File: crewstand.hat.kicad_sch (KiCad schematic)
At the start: 18 parts, among them J1 GPIO, J2 CAN Terminal, J3 Sensor Terminal, J4 V-In, J6 V-Out, J7 Relais2, J8 Relais1, U2 MCP2515-xSO, U3 MCP2551-I-P, U4 PicoW, Y2 12M

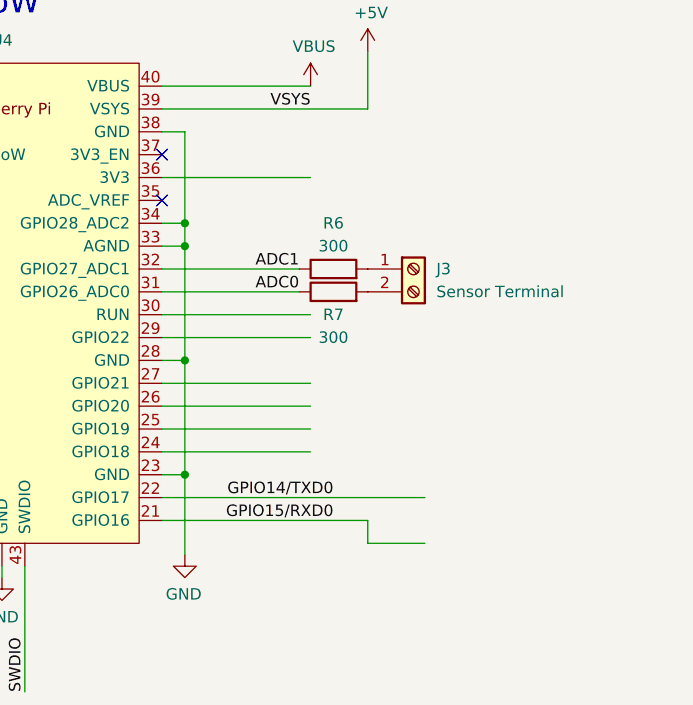
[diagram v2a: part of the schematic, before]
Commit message: fix(Sensors): correct resistor placement for analog sensor readings
- Move pull-down resistors from sensor-to-ADC path to ADC-to-GND
- Update schematic to implement proper current-to-voltage conversion

Breaking Change: Yes
- PCB layout updated
- Existing boards will need rework to implement this fix

Resolves: #6
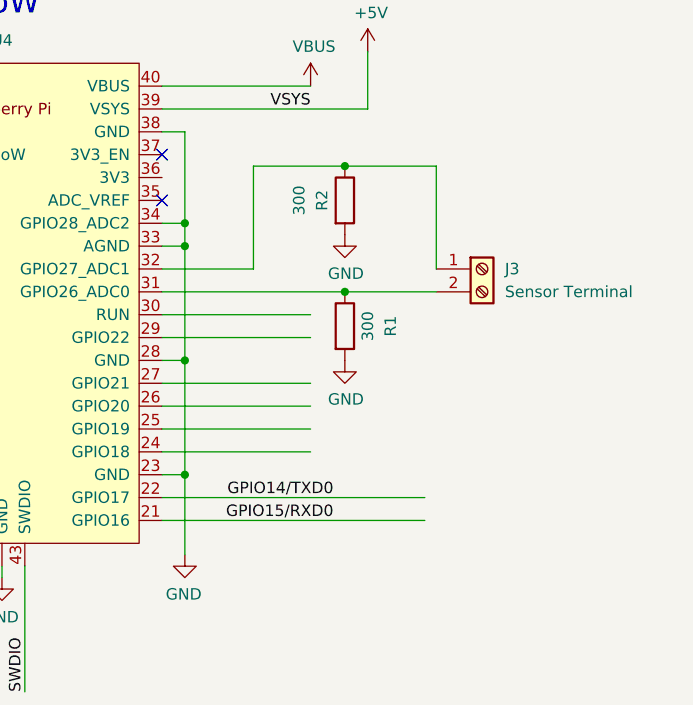
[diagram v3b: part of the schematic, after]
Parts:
- removed R6, R7: 300, Resistor_THT:R_Axial_DIN0204_L3.6mm_D1.6mm_P5.08mm_Horizontal, symbol Device:R
- added R1, R2: 300, Resistor_THT:R_Axial_DIN0204_L3.6mm_D1.6mm_P5.08mm_Horizontal, symbol Device:R
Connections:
- net ADC0 is gone; now on an unnamed net: U4.31 (GPIO26_ADC0)
- net ADC1 is gone; now on an unnamed net: U4.32 (GPIO27_ADC1)
- net GND: now also R1.2, R2.2
- net at J3.1 (Pin_1): now also R2.1
- net at J3.2 (Pin_2): now also R1.1
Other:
- moved on the sheet: J3
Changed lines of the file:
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@@
   (junction (at 179.07 128.27) (diameter 0) (color 0 0 0 0)
   )
+  (junction (at 259.08 38.1) (diameter 0) (color 0 0 0 0)
+  )
+  (junction (at 259.08 52.07) (diameter 0) (color 0 0 0 0)
+  )
   (no_connect (at 238.76 36.83))
   (no_connect (at 238.76 41.91))
@@
     (stroke (width 0) (type solid))
   )
+  (wire (pts (xy 248.92 38.1) (xy 259.08 38.1))
+    (stroke (width 0) (type default))
+  )
   (wire (pts (xy 96.52 125.73) (xy 104.14 125.73))
     (stroke (width 0) (type default))
@@
     (stroke (width 0) (type solid))
   )
+  (wire (pts (xy 248.92 38.1) (xy 248.92 49.53))
+    (stroke (width 0) (type default))
+  )
   (wire (pts (xy 60.96 30.48) (xy 31.75 30.48))
     (stroke (width 0) (type solid))
@@
     (stroke (width 0) (type solid))
   )
-  (wire (pts (xy 261.62 80.01) (xy 267.97 80.01))
-    (stroke (width 0) (type default))
-  )
-  (wire (pts (xy 261.62 77.47) (xy 261.62 80.01))
-    (stroke (width 0) (type default))
-  )
   (wire (pts (xy 73.66 40.64) (xy 100.33 40.64))
     (stroke (width 0) (type solid))
@@
     (stroke (width 0) (type solid))
   )
+  (wire (pts (xy 259.08 52.07) (xy 269.24 52.07))
+    (stroke (width 0) (type default))
+  )
   (wire (pts (xy 76.2 27.94) (xy 73.66 27.94))
     (stroke (width 0) (type solid))
@@
     (stroke (width 0) (type default))
   )
+  (wire (pts (xy 269.24 38.1) (xy 269.24 49.53))
+    (stroke (width 0) (type default))
+  )
   (wire (pts (xy 153.67 107.95) (xy 153.67 110.49))
     (stroke (width 0) (type default))
@@
     (stroke (width 0) (type default))
   )
-  (wire (pts (xy 238.76 49.53) (xy 254 49.53))
-    (stroke (width 0) (type default))
-  )
   (wire (pts (xy 31.75 45.72) (xy 60.96 45.72))
     (stroke (width 0) (type solid))
@@
     (stroke (width 0) (type default))
   )
+  (wire (pts (xy 238.76 49.53) (xy 248.92 49.53))
+    (stroke (width 0) (type default))
+  )
   (wire (pts (xy 31.75 71.12) (xy 60.96 71.12))
     (stroke (width 0) (type solid))
@@
     (stroke (width 0) (type default))
   )
-  (wire (pts (xy 238.76 39.37) (xy 255.27 39.37))
-    (stroke (width 0) (type default))
-  )
   (wire (pts (xy 166.37 118.11) (xy 166.37 119.38))
     (stroke (width 0) (type default))
@@
     (stroke (width 0) (type default))
   )
+  (wire (pts (xy 259.08 38.1) (xy 269.24 38.1))
+    (stroke (width 0) (type default))
+  )
   (wire (pts (xy 110.49 113.03) (xy 113.03 113.03))
     (stroke (width 0) (type default))
@@
     (stroke (width 0) (type solid))
   )
+  (wire (pts (xy 238.76 52.07) (xy 259.08 52.07))
+    (stroke (width 0) (type default))
+  )
   (wire (pts (xy 143.51 123.19) (xy 152.4 123.19))
     (stroke (width 0) (type default))
@@
     (stroke (width 0) (type default))
   )
-  (wire (pts (xy 238.76 52.07) (xy 254 52.07))
-    (stroke (width 0) (type default))
-  )
   (wire (pts (xy 116.84 69.85) (xy 129.54 69.85))
     (stroke (width 0) (type default))
   )
-  (wire (pts (xy 238.76 77.47) (xy 261.62 77.47))
+  (wire (pts (xy 238.76 77.47) (xy 267.97 77.47))
     (stroke (width 0) (type default))
   )
@@
     (effects (font (size 1.27 1.27)) (justify left bottom))
   )
-  (label "ADC1" (at 254 49.53 180) (fields_autoplaced)
-    (effects (font (size 1.27 1.27)) (justify right bottom))
-  )
   (label "ID_SCL" (at 100.33 60.96 180) (fields_autoplaced)
     (effects (font (size 1.27 1.27)) (justify right bottom))
@@
     (effects (font (size 1.27 1.27)) (justify right bottom))
   )
-  (label "ADC0" (at 254 52.07 180) (fields_autoplaced)
-    (effects (font (size 1.27 1.27)) (justify right bottom))
-  )
   (label "GPIO13{slash}PWM1" (at 31.75 68.58 0) (fields_autoplaced)
     (effects (font (size 1.27 1.27)) (justify left bottom))
@@
     )
   )
+  (symbol (lib_id "Device:R") (at 259.08 41.91 0) (unit 1)
+    (in_bom yes) (on_board yes) (dnp no)
+    (property "Reference" "R2" (at 256.54 41.91 90)
+      (effects (font (size 1.27 1.27)))
+    )
+    (property "Value" "300" (at 254 41.91 90)
+      (effects (font (size 1.27 1.27)))
+    )
+    (property "Footprint" "Resistor_THT:R_Axial_DIN0204_L3.6mm_D1.6mm_P5.08mm_Horizontal" (at 257.302 41.91 90)
+      (effects (font (size 1.27 1.27)) hide)
+    )
+    (property "Datasheet" "~" (at 259.08 41.91 0)
+      (effects (font (size 1.27 1.27)) hide)
+    )
+    (pin "1")
+    (pin "2")
+    (instances
+      (project "crewstand.hat"
+        (path "/e63e39d7-6ac0-4ffd-8aa3-1841a4541b55"
+          (reference "R2") (unit 1)
+        )
+      )
+    )
+  )
   (symbol (lib_id "RPi_Pico:PicoW") (at 220.98 53.34 0) (unit 1)
     (in_bom yes) (on_board yes) (dnp no)
@@
     )
   )
-  (symbol (lib_id "Connector:Screw_Terminal_01x02") (at 266.7 49.53 0) (unit 1)
-    (in_bom yes) (on_board yes) (dnp no) (fields_autoplaced)
-    (property "Reference" "J3" (at 269.24 49.53 0)
+  (symbol (lib_id "Connector:Screw_Terminal_01x02") (at 274.32 49.53 0) (unit 1)
+    (in_bom yes) (on_board yes) (dnp no)
+    (property "Reference" "J3" (at 276.86 49.53 0)
       (effects (font (size 1.27 1.27)) (justify left))
     )
-    (property "Value" "Sensor Terminal" (at 269.24 52.07 0)
+    (property "Value" "Sensor Terminal" (at 276.86 52.07 0)
       (effects (font (size 1.27 1.27)) (justify left))
     )
-    (property "Footprint" "TerminalBlock:TerminalBlock_bornier-2_P5.08mm" (at 266.7 49.53 0)
+    (property "Footprint" "TerminalBlock:TerminalBlock_bornier-2_P5.08mm" (at 274.32 49.53 0)
       (effects (font (size 1.27 1.27)) hide)
     )
-    (property "Datasheet" "~" (at 266.7 49.53 0)
+    (property "Datasheet" "~" (at 274.32 49.53 0)
       (effects (font (size 1.27 1.27)) hide)
     )
@@
     )
   )
-  (symbol (lib_id "Device:R") (at 257.81 52.07 90) (unit 1)
-    (in_bom yes) (on_board yes) (dnp no)
-    (property "Reference" "R7" (at 257.81 54.61 90)
-      (effects (font (size 1.27 1.27)))
-    )
-    (property "Value" "300" (at 257.81 57.15 90)
-      (effects (font (size 1.27 1.27)))
-    )
-    (property "Footprint" "Resistor_THT:R_Axial_DIN0204_L3.6mm_D1.6mm_P5.08mm_Horizontal" (at 257.81 53.848 90)
-      (effects (font (size 1.27 1.27)) hide)
-    )
-    (property "Datasheet" "~" (at 257.81 52.07 0)
-      (effects (font (size 1.27 1.27)) hide)
-    )
-    (pin "1")
-    (pin "2")
-    (instances
-      (project "crewstand.hat"
-        (path "/e63e39d7-6ac0-4ffd-8aa3-1841a4541b55"
-          (reference "R7") (unit 1)
-        )
-      )
-    )
-  )
   (symbol (lib_id "Connector:Screw_Terminal_01x02") (at 209.55 111.76 0) (unit 1)
     (in_bom yes) (on_board yes) (dnp no) (fields_autoplaced)
@@
     )
   )
+  (symbol (lib_id "Device:R") (at 259.08 55.88 0) (unit 1)
+    (in_bom yes) (on_board yes) (dnp no)
+    (property "Reference" "R1" (at 264.16 55.88 90)
+      (effects (font (size 1.27 1.27)))
+    )
+    (property "Value" "300" (at 261.62 55.88 90)
+      (effects (font (size 1.27 1.27)))
+    )
+    (property "Footprint" "Resistor_THT:R_Axial_DIN0204_L3.6mm_D1.6mm_P5.08mm_Horizontal" (at 257.302 55.88 90)
+      (effects (font (size 1.27 1.27)) hide)
+    )
+    (property "Datasheet" "~" (at 259.08 55.88 0)
+      (effects (font (size 1.27 1.27)) hide)
+    )
+    (pin "1")
+    (pin "2")
+    (instances
+      (project "crewstand.hat"
+        (path "/e63e39d7-6ac0-4ffd-8aa3-1841a4541b55"
+          (reference "R1") (unit 1)
+        )
+      )
+    )
+  )
   (symbol (lib_id "Connector_Generic:Conn_01x03") (at 134.62 54.61 0) (unit 1)
     (in_bom yes) (on_board yes) (dnp no) (fields_autoplaced)
@@
     )
   )
-  (symbol (lib_id "Device:R") (at 257.81 49.53 90) (unit 1)
+  (symbol (lib_id "power:GND") (at 259.08 59.69 0) (unit 1)
     (in_bom yes) (on_board yes) (dnp no)
-    (property "Reference" "R6" (at 257.81 44.45 90)
-      (effects (font (size 1.27 1.27)))
+    (property "Reference" "#PWR04" (at 259.08 66.04 0)
+      (effects (font (size 1.27 1.27)) hide)
     )
-    (property "Value" "300" (at 257.81 46.99 90)
+    (property "Value" "GND" (at 259.1943 64.0144 0)
       (effects (font (size 1.27 1.27)))
     )
-    (property "Footprint" "Resistor_THT:R_Axial_DIN0204_L3.6mm_D1.6mm_P5.08mm_Horizontal" (at 257.81 51.308 90)
-      (effects (font (size 1.27 1.27)) hide)
+    (property "Footprint" "" (at 259.08 59.69 0)
+      (effects (font (size 1.27 1.27)))
     )
-    (property "Datasheet" "~" (at 257.81 49.53 0)
-      (effects (font (size 1.27 1.27)) hide)
+    (property "Datasheet" "" (at 259.08 59.69 0)
+      (effects (font (size 1.27 1.27)))
     )
     (pin "1")
-    (pin "2")
     (instances
       (project "crewstand.hat"
         (path "/e63e39d7-6ac0-4ffd-8aa3-1841a4541b55"
-          (reference "R6") (unit 1)
+          (reference "#PWR04") (unit 1)
         )
       )
@@
         )
       )
+    )
+  )
+  (symbol (lib_id "power:GND") (at 259.08 45.72 0) (unit 1)
+    (in_bom yes) (on_board yes) (dnp no)
+    (property "Reference" "#PWR018" (at 259.08 52.07 0)
+      (effects (font (size 1.27 1.27)) hide)
+    )
+    (property "Value" "GND" (at 259.1943 50.0444 0)
+      (effects (font (size 1.27 1.27)))
+    )
+    (property "Footprint" "" (at 259.08 45.72 0)
+      (effects (font (size 1.27 1.27)))
+    )
+    (property "Datasheet" "" (at 259.08 45.72 0)
+      (effects (font (size 1.27 1.27)))
+    )
+    (pin "1")
+    (instances
+      (project "crewstand.hat"
+        (path "/e63e39d7-6ac0-4ffd-8aa3-1841a4541b55"
+          (reference "#PWR018") (unit 1)
+        )
+      )

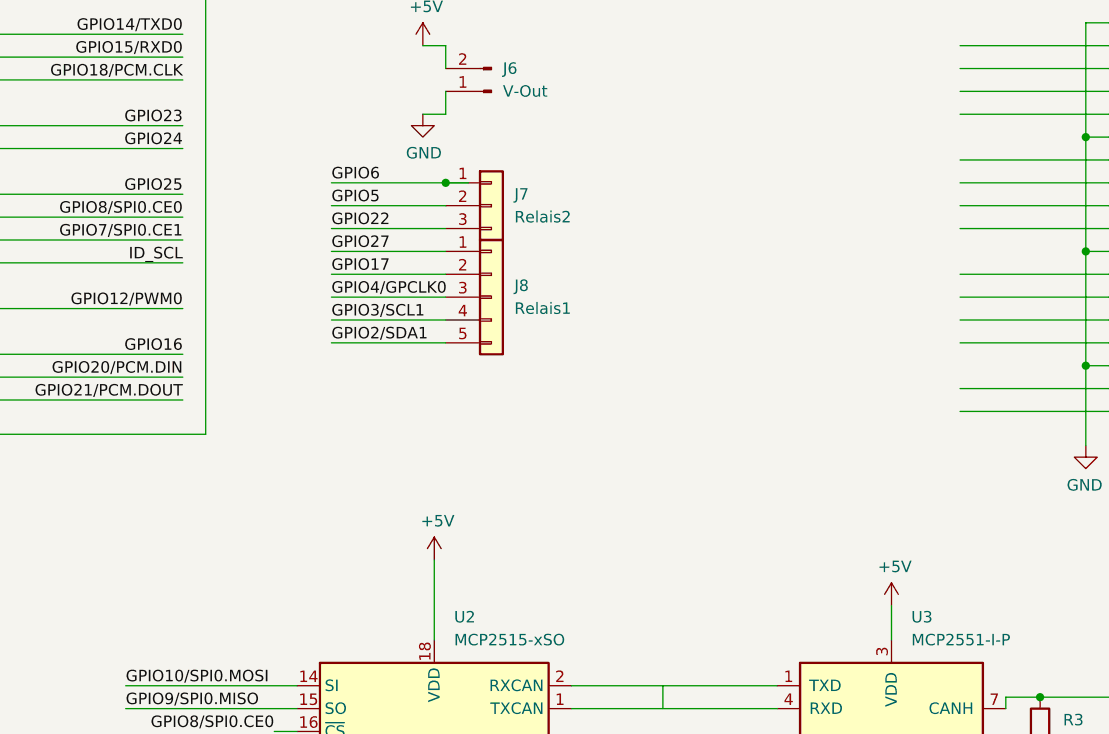
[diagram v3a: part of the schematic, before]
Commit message: feat: switch to professional PCB manufacturing service
- Update design rules for professional PCB manufacturing
- Prepare files for PCBWay or similar manufacturer submission
- use two layers for routing
    - use GND / 5V fill on layers
-  place silkscreen notes
- add redundant screw terminal for relais board connection

Resolves: #7
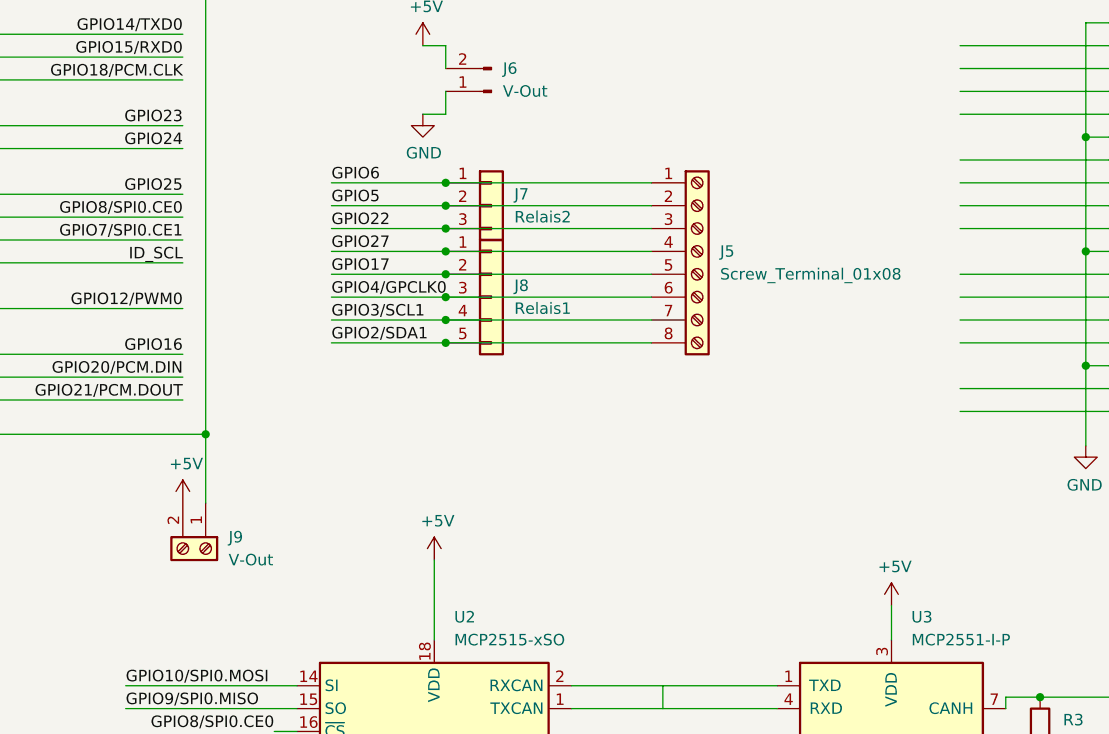
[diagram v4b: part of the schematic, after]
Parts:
- added J5: Screw_Terminal_01x08, TerminalBlock:TerminalBlock_bornier-8_P5.08mm, symbol Connector:Screw_Terminal_01x08
- added J9: V-Out, TerminalBlock:TerminalBlock_bornier-2_P5.08mm, symbol Connector:Screw_Terminal_01x02
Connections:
- net +5V: now also J9.2 (Pin_2)
- net GND: now also J9.1 (Pin_1)
- net GPIO17: now also J5.5 (Pin_5)
- net GPIO22: now also J5.3 (Pin_3)
- net GPIO27: now also J5.4 (Pin_4)
- net GPIO2/SDA1: now also J5.8 (Pin_8)
- net GPIO3/SCL1: now also J5.7 (Pin_7)
- net GPIO4/GPCLK0: now also J5.6 (Pin_6)
- net GPIO5: now also J5.2 (Pin_2)
- net GPIO6: now also J5.1 (Pin_1)
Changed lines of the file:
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@@
   (junction (at 104.14 125.73) (diameter 0) (color 0 0 0 0)
   )
+  (junction (at 129.54 57.15) (diameter 0) (color 0 0 0 0)
+  )
+  (junction (at 129.54 62.23) (diameter 0) (color 0 0 0 0)
+  )
   (junction (at 76.2 27.94) (diameter 1.016) (color 0 0 0 0)
   )
@@
   (junction (at 81.28 133.35) (diameter 0) (color 0 0 0 0)
   )
+  (junction (at 129.54 54.61) (diameter 0) (color 0 0 0 0)
+  )
   (junction (at 241.3 46.99) (diameter 0) (color 0 0 0 0)
   )
+  (junction (at 129.54 59.69) (diameter 0) (color 0 0 0 0)
+  )
   (junction (at 58.42 58.42) (diameter 1.016) (color 0 0 0 0)
   )
   (junction (at 195.58 109.22) (diameter 0) (color 0 0 0 0)
   )
+  (junction (at 129.54 69.85) (diameter 0) (color 0 0 0 0)
+  )
   (junction (at 76.2 80.01) (diameter 0) (color 0 0 0 0)
   )
   (junction (at 76.2 68.58) (diameter 1.016) (color 0 0 0 0)
   )
+  (junction (at 129.54 64.77) (diameter 0) (color 0 0 0 0)
+  )
   (junction (at 195.58 116.84) (diameter 0) (color 0 0 0 0)
   )
@@
   (junction (at 179.07 128.27) (diameter 0) (color 0 0 0 0)
   )
+  (junction (at 129.54 67.31) (diameter 0) (color 0 0 0 0)
+  )
   (junction (at 259.08 38.1) (diameter 0) (color 0 0 0 0)
   )
   (junction (at 259.08 52.07) (diameter 0) (color 0 0 0 0)
+  )
+  (junction (at 102.87 80.01) (diameter 0) (color 0 0 0 0)
   )
   (no_connect (at 238.76 36.83))
@@
     (stroke (width 0) (type solid))
   )
+  (wire (pts (xy 129.54 67.31) (xy 152.4 67.31))
+    (stroke (width 0) (type default))
+  )
   (wire (pts (xy 203.2 59.69) (xy 200.66 59.69))
     (stroke (width 0) (type default))
@@
     (stroke (width 0) (type default))
   )
+  (wire (pts (xy 129.54 54.61) (xy 152.4 54.61))
+    (stroke (width 0) (type default))
+  )
   (wire (pts (xy 58.42 38.1) (xy 58.42 58.42))
     (stroke (width 0) (type solid))
@@
     (stroke (width 0) (type default))
   )
-  (wire (pts (xy 132.08 52.07) (xy 129.54 52.07))
+  (wire (pts (xy 129.54 52.07) (xy 152.4 52.07))
     (stroke (width 0) (type default))
   )
@@
     (stroke (width 0) (type default))
   )
+  (wire (pts (xy 102.87 80.01) (xy 102.87 87.63))
+    (stroke (width 0) (type default))
+  )
   (wire (pts (xy 31.75 33.02) (xy 60.96 33.02))
     (stroke (width 0) (type solid))
@@
     (stroke (width 0) (type default))
   )
+  (wire (pts (xy 129.54 69.85) (xy 152.4 69.85))
+    (stroke (width 0) (type default))
+  )
   (wire (pts (xy 76.2 24.13) (xy 76.2 27.94))
     (stroke (width 0) (type solid))
@@
     (stroke (width 0) (type default))
   )
+  (wire (pts (xy 129.54 59.69) (xy 152.4 59.69))
+    (stroke (width 0) (type default))
+  )
   (wire (pts (xy 73.66 38.1) (xy 100.33 38.1))
     (stroke (width 0) (type solid))
@@
     (stroke (width 0) (type default))
   )
+  (wire (pts (xy 129.54 62.23) (xy 152.4 62.23))
+    (stroke (width 0) (type default))
+  )
   (wire (pts (xy 31.75 45.72) (xy 60.96 45.72))
     (stroke (width 0) (type solid))
@@
     (stroke (width 0) (type solid))
   )
+  (wire (pts (xy 129.54 57.15) (xy 152.4 57.15))
+    (stroke (width 0) (type default))
+  )
   (wire (pts (xy 81.28 133.35) (xy 88.9 133.35))
     (stroke (width 0) (type default))
@@
   )
   (wire (pts (xy 110.49 128.27) (xy 113.03 128.27))
+    (stroke (width 0) (type default))
+  )
+  (wire (pts (xy 129.54 64.77) (xy 152.4 64.77))
     (stroke (width 0) (type default))
   )
@@
     )
   )
+  (symbol (lib_id "power:+5V") (at 100.33 87.63 0) (unit 1)
+    (in_bom yes) (on_board yes) (dnp no)
+    (property "Reference" "#PWR019" (at 100.33 91.44 0)
+      (effects (font (size 1.27 1.27)) hide)
+    )
+    (property "Value" "+5V" (at 100.6983 83.3056 0)
+      (effects (font (size 1.27 1.27)))
+    )
+    (property "Footprint" "" (at 100.33 87.63 0)
+      (effects (font (size 1.27 1.27)))
+    )
+    (property "Datasheet" "" (at 100.33 87.63 0)
+      (effects (font (size 1.27 1.27)))
+    )
+    (pin "1")
+    (instances
+      (project "crewstand.hat"
+        (path "/e63e39d7-6ac0-4ffd-8aa3-1841a4541b55"
+          (reference "#PWR019") (unit 1)
+        )
+      )
+    )
+  )
   (symbol (lib_id "Device:R") (at 259.08 41.91 0) (unit 1)
     (in_bom yes) (on_board yes) (dnp no)
@@
     )
   )
+  (symbol (lib_id "Connector:Screw_Terminal_01x08") (at 157.48 59.69 0) (unit 1)
+    (in_bom yes) (on_board yes) (dnp no) (fields_autoplaced)
+    (property "Reference" "J5" (at 160.02 59.69 0)
+      (effects (font (size 1.27 1.27)) (justify left))
+    )
+    (property "Value" "Screw_Terminal_01x08" (at 160.02 62.23 0)
+      (effects (font (size 1.27 1.27)) (justify left))
+    )
+    (property "Footprint" "TerminalBlock:TerminalBlock_bornier-8_P5.08mm" (at 157.48 59.69 0)
+      (effects (font (size 1.27 1.27)) hide)
+    )
+    (property "Datasheet" "~" (at 157.48 59.69 0)
+      (effects (font (size 1.27 1.27)) hide)
+    )
+    (pin "6")
+    (pin "3")
+    (pin "1")
+    (pin "2")
+    (pin "8")
+    (pin "4")
+    (pin "5")
+    (pin "7")
+    (instances
+      (project "crewstand.hat"
+        (path "/e63e39d7-6ac0-4ffd-8aa3-1841a4541b55"
+          (reference "J5") (unit 1)
+        )
+      )
+    )
+  )
   (symbol (lib_id "Connector:Screw_Terminal_01x02") (at 100.33 19.05 90) (unit 1)
     (in_bom yes) (on_board yes) (dnp no) (fields_autoplaced)
@@
         )
       )
+    )
+  )
+  (symbol (lib_id "Connector:Screw_Terminal_01x02") (at 102.87 92.71 270) (unit 1)
+    (in_bom yes) (on_board yes) (dnp no) (fields_autoplaced)
+    (property "Reference" "J9" (at 105.41 91.44 90)
+      (effects (font (size 1.27 1.27)) (justify left))
+    )
+    (property "Value" "V-Out" (at 105.41 93.98 90)
+      (effects (font (size 1.27 1.27)) (justify left))
+    )
+    (property "Footprint" "TerminalBlock:TerminalBlock_bornier-2_P5.08mm" (at 102.87 92.71 0)
+      (effects (font (size 1.27 1.27)) hide)
+    )
+    (property "Datasheet" "~" (at 102.87 92.71 0)
+      (effects (font (size 1.27 1.27)) hide)
+    )
+    (pin "1")
+    (pin "2")
+    (instances
+      (project "crewstand.hat"
+        (path "/e63e39d7-6ac0-4ffd-8aa3-1841a4541b55"
+          (reference "J9") (unit 1)
+        )
+      )
